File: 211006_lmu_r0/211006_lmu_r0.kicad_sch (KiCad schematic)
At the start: 4 parts, among them J1 Conn_02x03_Odd_Even, J2 Conn_02x03_Odd_Even, J3 Conn_02x08_Odd_Even, J4 Conn_01x13

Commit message: Updated lmu project with relative library paths and fixed broken symbols
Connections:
- net GND: now reaches J3.10 (Pin_10), J3.12 (Pin_12), J3.14 (Pin_14), J3.16 (Pin_16), J3.2 (Pin_2), J3.4 (Pin_4), J3.6 (Pin_6), J3.8 (Pin_8)
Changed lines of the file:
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@@
       (effects (font (size 1.27 1.27)) hide)
     )
+    (pin "1")
   )
   (symbol (lib_id "Connector_Generic:Conn_01x13") (at 267.97 87.63 0) (unit 1)

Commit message: Updated some components to make sourcing easier
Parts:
- J1, J2: Manufacturer (none) -> Molex; Part Number (none) -> 462071006
- J3: Part Number (none) -> -
- J4: Manufacturer (none) -> -; Part Number (none) -> -
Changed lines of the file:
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@@
+      (effects (font (size 1.27 1.27)) hide)
+    )
+    (property "Part Number" "-" (id 4) (at 267.97 87.63 0)
+      (effects (font (size 1.27 1.27)) hide)
+    )
+    (property "Manufacturer" "-" (id 5) (at 267.97 87.63 0)
       (effects (font (size 1.27 1.27)) hide)
     )
@@
       (effects (font (size 1.27 1.27)) hide)
     )
+    (property "Manufacturer" "Molex" (id 4) (at 45.72 30.48 0)
+      (effects (font (size 1.27 1.27)) hide)
+    )
+    (property "Part Number" "462071006" (id 5) (at 45.72 30.48 0)
+      (effects (font (size 1.27 1.27)) hide)
+    )
     (pin "1")
     (pin "2")
@@
       (effects (font (size 1.27 1.27)) hide)
     )
+    (property "Manufacturer" "Molex" (id 4) (at 45.72 44.45 0)
+      (effects (font (size 1.27 1.27)) hide)
+    )
+    (property "Part Number" "462071006" (id 5) (at 45.72 44.45 0)
+      (effects (font (size 1.27 1.27)) hide)
+    )
     (pin "1")
     (pin "2")
@@
     )
     (property "Datasheet" "~" (id 3) (at 267.97 46.99 0)
+      (effects (font (size 1.27 1.27)) hide)
+    )
+    (property "Part Number" "-" (id 4) (at 267.97 46.99 0)
+      (effects (font (size 1.27 1.27)) hide)
+    )
+    (property "Manufacturer" "" (id 5) (at 267.97 46.99 0)
       (effects (font (size 1.27 1.27)) hide)
     )
@@
       (reference "#PWR086") (unit 1) (value "GND_ISO") (footprint "")
     )
-    (path "/00000000-0000-0000-0000-0000615d6dd3/00000000-0000-0000-0000-000061688149"
-      (reference "#PWR087") (unit 1) (value "GND_ISO") (footprint "")
+    (path "/00000000-0000-0000-0000-0000615d6dd3/1b82c90c-8eb2-4d7e-90bd-08ff4ac0d81b"
+      (reference "#PWR087") (unit 1) (value "+3V3_ISO") (footprint "")
     )
     (path "/00000000-0000-0000-0000-0000615d6dd3/00000000-0000-0000-0000-000061687b4c"
@@
       (reference "#PWR095") (unit 1) (value "GND_ISO") (footprint "")
     )
+    (path "/00000000-0000-0000-0000-0000615d6dd3/6924b9c0-bd5f-481d-9f8d-7fc20978c5ab"
+      (reference "#PWR096") (unit 1) (value "GND_ISO") (footprint "")
+    )
+    (path "/00000000-0000-0000-0000-0000615d6dd3/3fda080e-f768-4619-ba3c-beddd1d2b960"
+      (reference "#PWR097") (unit 1) (value "+3V3_ISO") (footprint "")
+    )
+    (path "/00000000-0000-0000-0000-0000615d6dd3/e3b914a8-68f7-4ef2-b944-05204da163e8"
+      (reference "#PWR098") (unit 1) (value "GND_ISO") (footprint "")
+    )
     (path "/00000000-0000-0000-0000-0000615d6d63/00000000-0000-0000-0000-00006165b450"
       (reference "C1") (unit 1) (value "220uF") (footprint "Capacitor_SMD:CP_Elec_10x12.5")
@@
       (reference "J12") (unit 1) (value "Conn_01x03") (footprint "Connector_PinHeader_2.54mm:PinHeader_1x03_P2.54mm_Vertical")
     )
+    (path "/00000000-0000-0000-0000-0000615d6dd3/b3ac3a03-f013-4d1d-b3c1-6416cab3ed78"
+      (reference "J13") (unit 1) (value "Conn_02x03_Odd_Even") (footprint "Connector_PinHeader_2.54mm:PinHeader_2x03_P2.54mm_Vertical")
+    )
     (path "/00000000-0000-0000-0000-000061643001/00000000-0000-0000-0000-000061647a5a"
       (reference "K1") (unit 1) (value "G5V-2") (footprint "Relay_THT:Relay_DPDT_Omron_G5V-2")
@@
     )
     (path "/00000000-0000-0000-0000-0000615d6dd3/00000000-0000-0000-0000-0000615e56df"
-      (reference "SW1") (unit 1) (value "SW_Push") (footprint "Button_Switch_SMD:SW_SPST_Omron_B3FS-100xP")
-    )
-    (path "/00000000-0000-0000-0000-0000615d6dd3/00000000-0000-0000-0000-0000615e825f"
-      (reference "SW2") (unit 1) (value "SW_SPST") (footprint "Button_Switch_SMD:SW_DIP_SPSTx01_Slide_9.78x4.72mm_W8.61mm_P2.54mm")
+      (reference "SW1") (unit 1) (value "SW_Push") (footprint "Button_Switch_SMD:SW_SPST_SKQG_WithStem")
     )
     (path "/00000000-0000-0000-0000-000061619f34/00000000-0000-0000-0000-00006161ac01/00000000-0000-0000-0000-00006234dcc2/00000000-0000-0000-0000-00006234dcaa"

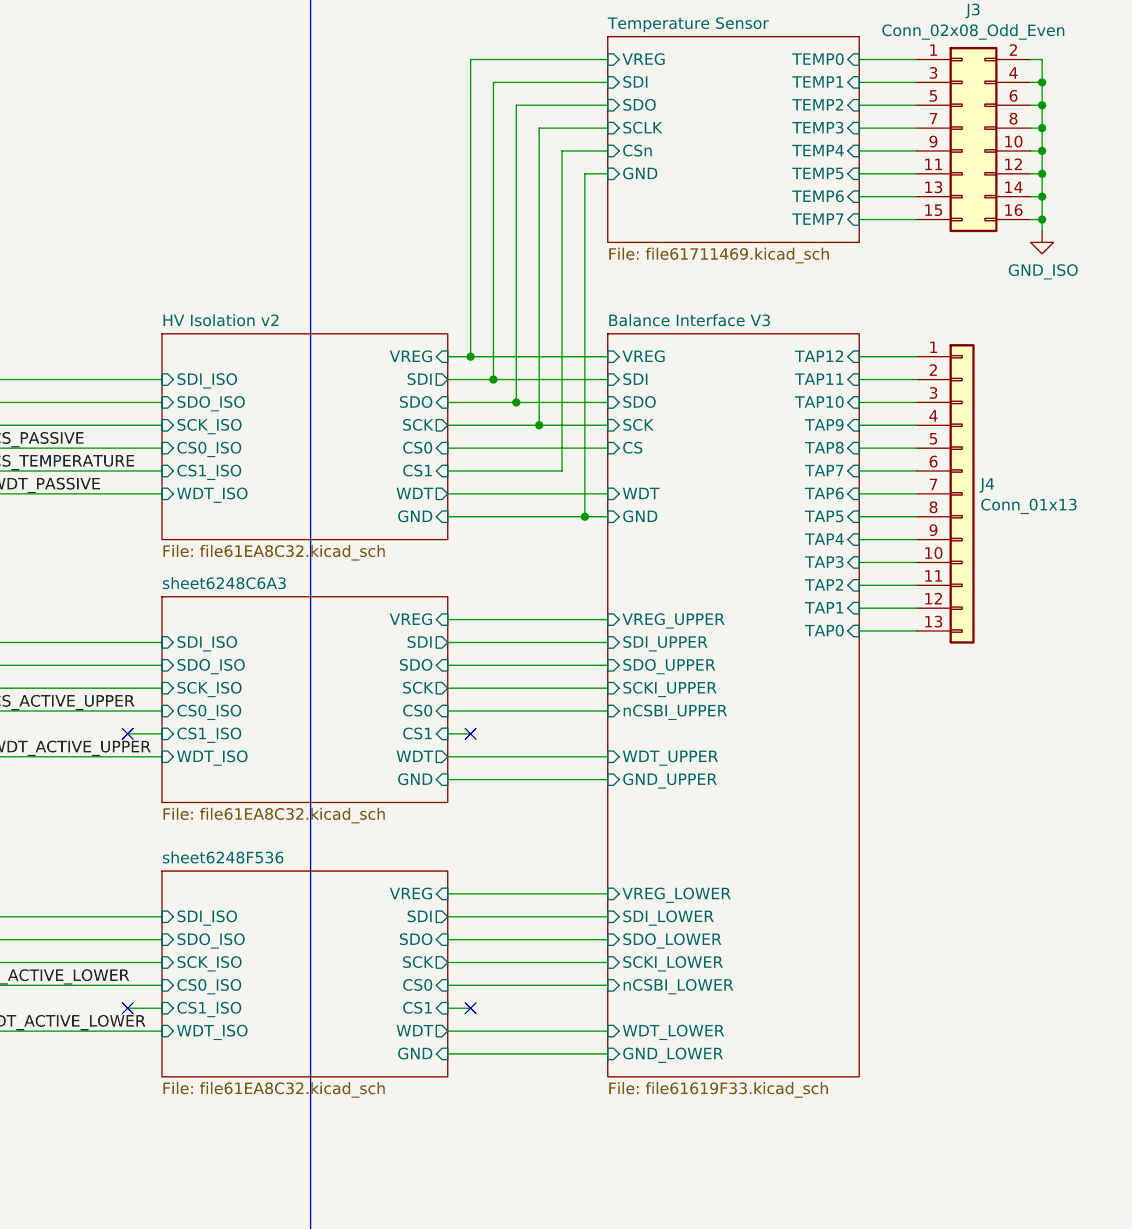
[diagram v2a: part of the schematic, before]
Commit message: fixed footprints for headers, started planning out zones
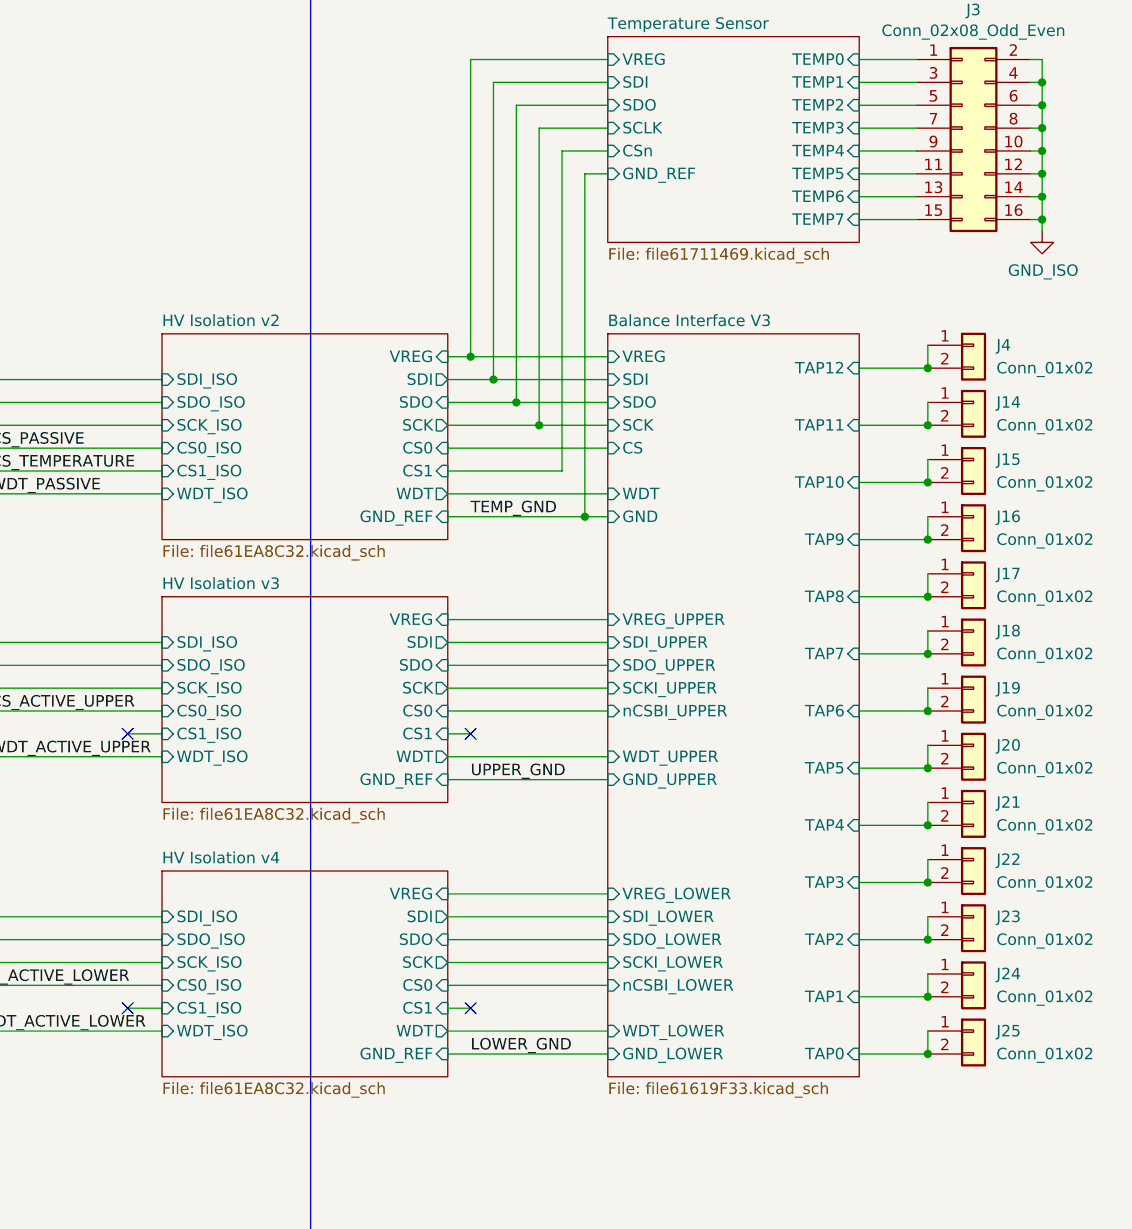
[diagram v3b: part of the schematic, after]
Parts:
- removed J4: Conn_01x13, symbol Connector_Generic:Conn_01x13
- added J14, J15, J16, J17, J18, J19, J20, J21, J22, J23, J24, J25, J4: Conn_01x02, Connector_Molex:Molex_Mini-Fit_Jr_5566-02A_2x01_P4.20mm_Vertical, symbol Connector_Generic:Conn_01x02
- J3: footprint (none) -> Connector_Molex:Molex_Mini-Fit_Jr_5566-16A_2x08_P4.20mm_Vertical; Manufacturer (none) -> Molex; Part Number - -> 46015-1603
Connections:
- net Balance Interface V3/TAP0: now also J25.1 (Pin_1), J25.2 (Pin_2)
- net Balance Interface V3/TAP1: now also J24.1 (Pin_1), J24.2 (Pin_2)
- net Balance Interface V3/TAP10: now also J15.1 (Pin_1), J15.2 (Pin_2)
- net Balance Interface V3/TAP11: now also J14.1 (Pin_1), J14.2 (Pin_2)
- net Balance Interface V3/TAP12: now also J4.1 (Pin_1), J4.2 (Pin_2)
- net Balance Interface V3/TAP2: now also J23.1 (Pin_1), J23.2 (Pin_2)
- net Balance Interface V3/TAP3: now also J22.1 (Pin_1), J22.2 (Pin_2)
- net Balance Interface V3/TAP4: now also J21.1 (Pin_1), J21.2 (Pin_2)
- net Balance Interface V3/TAP5: now also J20.1 (Pin_1), J20.2 (Pin_2)
- net Balance Interface V3/TAP6: now also J19.1 (Pin_1), J19.2 (Pin_2)
- net Balance Interface V3/TAP7: now also J18.1 (Pin_1), J18.2 (Pin_2)
- net Balance Interface V3/TAP8: now also J17.1 (Pin_1), J17.2 (Pin_2)
- net Balance Interface V3/TAP9: now also J16.1 (Pin_1), J16.2 (Pin_2)
- net GND renamed GND_ISO
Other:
- removed sheet sheet6248C6A3
- removed sheet sheet6248F536
- added sheet HV Isolation v3 (file61EA8C32.kicad_sch)
- added sheet HV Isolation v4 (file61EA8C32.kicad_sch)
- sheet HV Isolation v2 ports: added GND_REF; removed GND
- sheet Temperature Sensor ports: added GND_REF; removed GND

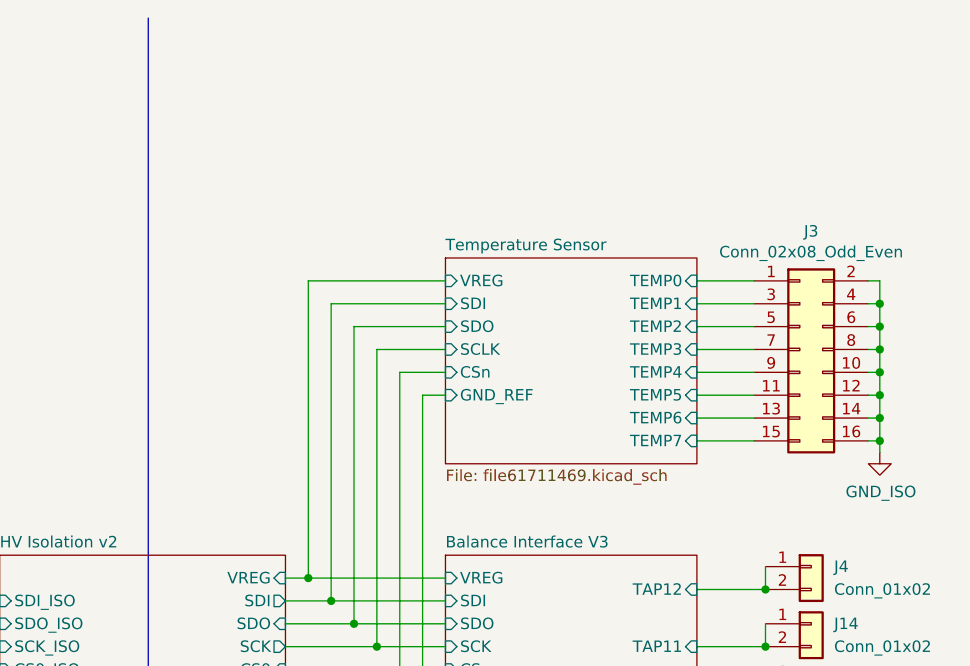
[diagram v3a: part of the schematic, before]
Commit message: Lots of routing and placing, according to planned layout
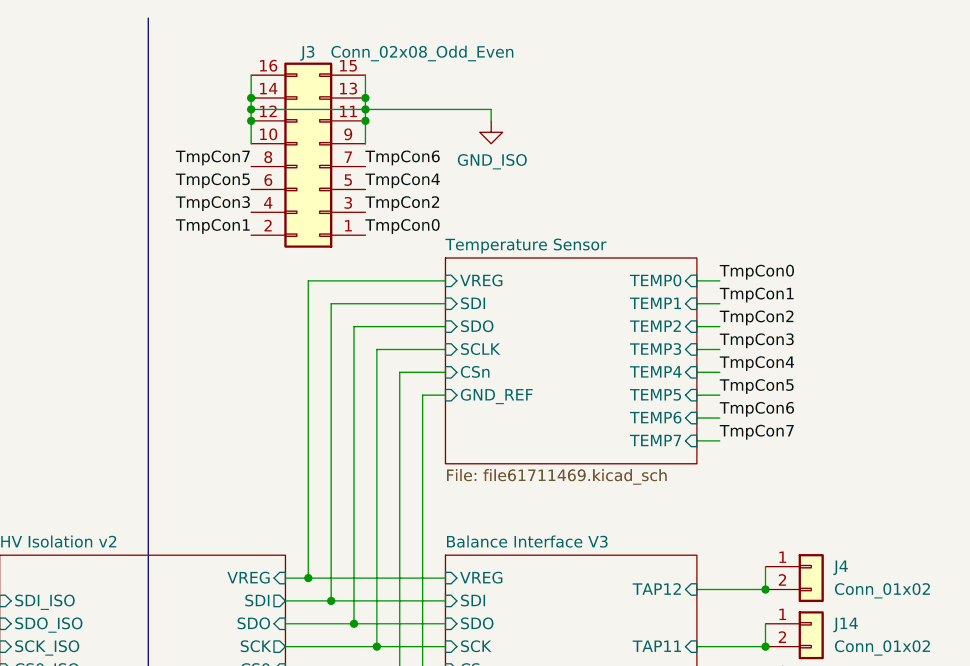
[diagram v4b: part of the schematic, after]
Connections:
- net Temperature Sensor/TEMP4 is gone; now on net GND_ISO: J3.9 (Pin_9)
- net Temperature Sensor/TEMP5 is gone; now on net GND_ISO: J3.11 (Pin_11)
- net Temperature Sensor/TEMP6 is gone; now on net GND_ISO: J3.13 (Pin_13)
- net Temperature Sensor/TEMP7 is gone; now on net GND_ISO: J3.15 (Pin_15)
- net GND_ISO: no longer J3.2 (Pin_2), J3.4 (Pin_4), J3.6 (Pin_6), J3.8 (Pin_8)
- net Temperature Sensor/TEMP0 renamed TmpCon0
- net Temperature Sensor/TEMP1 renamed TmpCon2
- net Temperature Sensor/TEMP2 renamed TmpCon4
- net Temperature Sensor/TEMP3 renamed TmpCon6
- new net TmpCon1: J3.2 (Pin_2)
- new net TmpCon3: J3.4 (Pin_4)
- new net TmpCon5: J3.6 (Pin_6)
- new net TmpCon7: J3.8 (Pin_8)
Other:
- moved on the sheet: J3

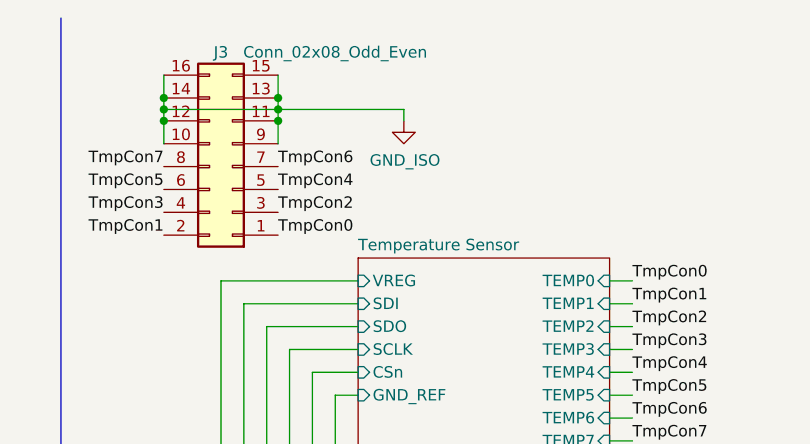
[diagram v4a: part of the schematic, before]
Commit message: CAN transceiver stuff almost done, still needs CAN_S finished
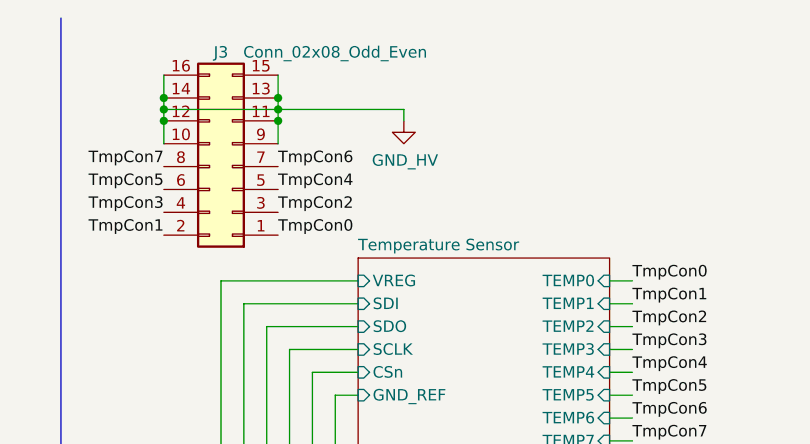
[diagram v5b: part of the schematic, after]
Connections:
- net GND_ISO renamed GND_HV
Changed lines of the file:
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@@
     (effects (font (size 1.27 1.27)) (justify left bottom))
-  )
-  (symbol (lib_id "gnd_iso:GND_ISO") (at 233.68 21.59 0) (unit 1)
-    (in_bom yes) (on_board yes)
-    (property "Reference" "#PWR01" (id 0) (at 233.68 27.94 0)
-      (effects (font (size 1.27 1.27)) hide)
-    )
-    (property "Value" "GND_ISO" (id 1) (at 233.807 25.9842 0))
-    (property "Footprint" "" (id 2) (at 233.68 21.59 0)
-      (effects (font (size 1.27 1.27)) hide)
-    )
-    (property "Datasheet" "" (id 3) (at 233.68 21.59 0)
-      (effects (font (size 1.27 1.27)) hide)
-    )
-    (pin "1")
   )
   (symbol (lib_id "Connector_Generic:Conn_02x03_Odd_Even") (at 45.72 30.48 0) (unit 1)
@@
     (pin "1")
     (pin "2")
+  )
+  (symbol (lib_name "GND_HV_12") (lib_id "gnd_hv:GND_HV") (at 233.68 21.59 0) (unit 1)
+    (in_bom yes) (on_board yes)
+    (property "Reference" "#PWR0121" (id 0) (at 233.68 27.94 0)
+      (effects (font (size 1.27 1.27)) hide)
+    )
+    (property "Value" "GND_HV" (id 1) (at 233.807 25.9842 0))
+    (property "Footprint" "" (id 2) (at 233.68 21.59 0)
+      (effects (font (size 1.27 1.27)) hide)
+    )
+    (property "Datasheet" "" (id 3) (at 233.68 21.59 0)
+      (effects (font (size 1.27 1.27)) hide)
+    )
+    (pin "1")
   )
   (symbol (lib_id "Connector_Generic:Conn_01x02") (at 269.24 115.57 0) (unit 1)
@@
   )
   (symbol_instances
-    (path "/00000000-0000-0000-0000-000061694729"
-      (reference "#PWR01") (unit 1) (value "GND_ISO") (footprint "")
-    )
     (path "/00000000-0000-0000-0000-0000615d6d63/00000000-0000-0000-0000-000061665f18"
       (reference "#PWR02") (unit 1) (value "GND") (footprint "")
@@
       (reference "#PWR0120") (unit 1) (value "GND_HV") (footprint "")
     )
+    (path "/528bc8a8-b258-4259-b2bb-b454adde3a4a"
+      (reference "#PWR0121") (unit 1) (value "GND_HV") (footprint "")
+    )
     (path "/00000000-0000-0000-0000-00006171146a/00000000-0000-0000-0000-0000616cf5c8/f39239ac-c5ca-45ed-acd9-be3ff97551b4"
